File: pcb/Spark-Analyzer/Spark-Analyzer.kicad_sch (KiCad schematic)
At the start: 8 parts, among them J3 KF350-3.5-2P

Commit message: Updated name to Spark Analyzer
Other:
- title: PowerPod -> Spark Analyzer
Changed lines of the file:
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@@
   (paper "A3")
   (title_block
-    (title "PowerPod")
-    (date "2023-04-18")
-    (rev "A")
+    (title "Spark Analyzer")
+    (date "2023-10-06")
+    (rev "B")
   )
   (junction (at 162.56 77.47) (diameter 0) (color 0 0 0 0)
@@
     (pin "1")
     (instances
-      (project "PowerPod"
+      (project "Spark-Analyzer"
         (path "/e63e39d7-6ac0-4ffd-8aa3-1841a4541b55"
           (reference "#PWR04") (unit 1)
@@
     (pin "1")
     (instances
-      (project "PowerPod"
+      (project "Spark-Analyzer"
         (path "/e63e39d7-6ac0-4ffd-8aa3-1841a4541b55"
           (reference "#PWR031") (unit 1)
@@
     (pin "2")
     (instances
-      (project "PowerPod"
+      (project "Spark-Analyzer"
         (path "/e63e39d7-6ac0-4ffd-8aa3-1841a4541b55"
           (reference "J3") (unit 1)
@@
     )
     (instances
-      (project "PowerPod"
+      (project "Spark-Analyzer"
         (path "/e63e39d7-6ac0-4ffd-8aa3-1841a4541b55"
           (reference "H4") (unit 1)
@@
     (pin "1")
     (instances
-      (project "PowerPod"
+      (project "Spark-Analyzer"
         (path "/e63e39d7-6ac0-4ffd-8aa3-1841a4541b55/dc0e84e0-adcd-432b-9bb1-644eba2790b5"
           (reference "TP5") (unit 1)
@@
     )
     (instances
-      (project "PowerPod"
+      (project "Spark-Analyzer"
         (path "/e63e39d7-6ac0-4ffd-8aa3-1841a4541b55"
           (reference "H1") (unit 1)
@@
     (pin "1")
     (instances
-      (project "PowerPod"
+      (project "Spark-Analyzer"
         (path "/e63e39d7-6ac0-4ffd-8aa3-1841a4541b55"
           (reference "#PWR01") (unit 1)
@@
     )
     (instances
-      (project "PowerPod"
+      (project "Spark-Analyzer"
         (path "/e63e39d7-6ac0-4ffd-8aa3-1841a4541b55"
           (reference "H2") (unit 1)
@@
     (pin "2")
     (instances
-      (project "PowerPod"
+      (project "Spark-Analyzer"
         (path "/e63e39d7-6ac0-4ffd-8aa3-1841a4541b55/8b971fa9-4de7-4202-8255-0a278e8cf0e6"
           (reference "C21") (unit 1)
@@
     (pin "2")
     (instances
-      (project "PowerPod"
+      (project "Spark-Analyzer"
         (path "/e63e39d7-6ac0-4ffd-8aa3-1841a4541b55/8b971fa9-4de7-4202-8255-0a278e8cf0e6"
           (reference "C21") (unit 1)
@@
     )
     (instances
-      (project "PowerPod"
+      (project "Spark-Analyzer"
         (path "/e63e39d7-6ac0-4ffd-8aa3-1841a4541b55"
           (reference "H3") (unit 1)
@@
     )
     (instances
-      (project "PowerPod"
+      (project "Spark-Analyzer"
         (path "/e63e39d7-6ac0-4ffd-8aa3-1841a4541b55" (page "4"))
       )
@@
     )
     (instances
-      (project "PowerPod"
+      (project "Spark-Analyzer"
         (path "/e63e39d7-6ac0-4ffd-8aa3-1841a4541b55" (page "2"))
       )
@@
     )
     (instances
-      (project "PowerPod"
+      (project "Spark-Analyzer"
         (path "/e63e39d7-6ac0-4ffd-8aa3-1841a4541b55" (page "5"))
       )
@@
     )
     (instances
-      (project "PowerPod"
+      (project "Spark-Analyzer"
         (path "/e63e39d7-6ac0-4ffd-8aa3-1841a4541b55" (page "3"))
       )

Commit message: First app release and updated PCBA
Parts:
- removed TP5: TestPoint, TestPoint:TestPoint_Pad_D1.0mm, symbol Connector:TestPoint
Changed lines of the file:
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@@
   (junction (at 179.07 77.47) (diameter 0) (color 0 0 0 0)
   )
-  (junction (at 241.3 124.46) (diameter 0) (color 0 0 0 0)
-  )
   (junction (at 280.035 124.46) (diameter 0) (color 0 0 0 0)
   )
@@
     (stroke (width 0) (type default))
   )
-  (wire (pts (xy 241.3 114.935) (xy 241.3 124.46))
-    (stroke (width 0) (type default))
-  )
   (wire (pts (xy 280.035 124.46) (xy 299.72 124.46))
     (stroke (width 0) (type default))
@@
     (stroke (width 0) (type default))
   )
-  (wire (pts (xy 241.3 124.46) (xy 264.795 124.46))
-    (stroke (width 0) (type default))
-  )
   (wire (pts (xy 156.21 99.06) (xy 163.195 99.06))
     (stroke (width 0) (type default))
@@
     (stroke (width 0) (type default))
   )
-  (wire (pts (xy 216.535 124.46) (xy 241.3 124.46))
+  (wire (pts (xy 216.535 124.46) (xy 264.795 124.46))
     (stroke (width 0) (type default))
   )
@@
         )
       )
-    )
-  )
-  (symbol (lib_id "Connector:TestPoint") (at 241.3 114.935 0) (unit 1)
-    (in_bom yes) (on_board yes) (dnp no) (fields_autoplaced)
-    (property "Reference" "TP5" (at 242.697 110.9893 0)
-      (effects (font (size 1.27 1.27)) (justify left))
-    )
-    (property "Value" "TestPoint" (at 242.697 112.9103 0)
-      (effects (font (size 1.27 1.27)) (justify left))
-    )
-    (property "Footprint" "TestPoint:TestPoint_Pad_D1.0mm" (at 246.38 114.935 0)
-      (effects (font (size 1.27 1.27)) hide)
-    )
-    (property "Datasheet" "~" (at 246.38 114.935 0)
-      (effects (font (size 1.27 1.27)) hide)
-    )
-    (pin "1")
-    (instances
-      (project "Spark-Analyzer"
-        (path "/e63e39d7-6ac0-4ffd-8aa3-1841a4541b55/dc0e84e0-adcd-432b-9bb1-644eba2790b5"
-          (reference "TP5") (unit 1)
-        )
-        (path "/e63e39d7-6ac0-4ffd-8aa3-1841a4541b55"
-          (reference "TP9") (unit 1)
-        )
-      )

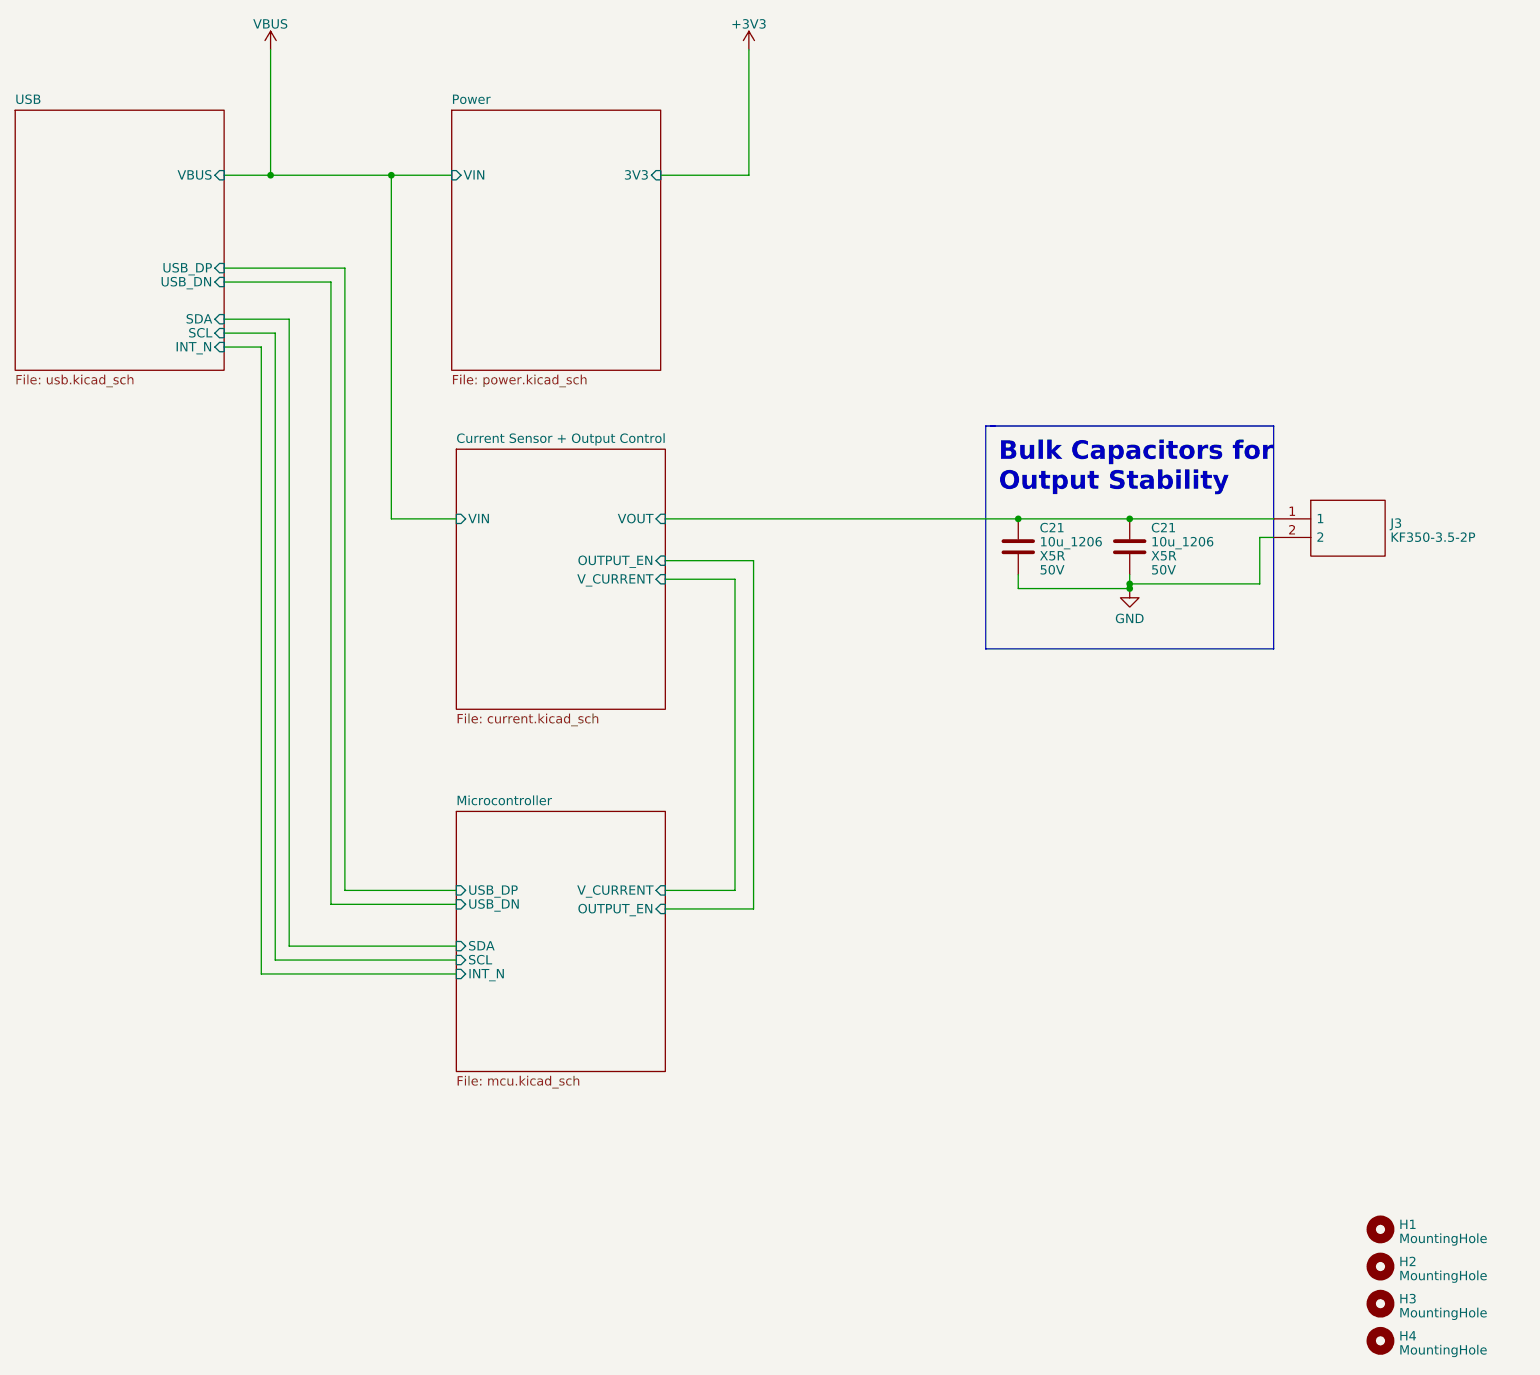
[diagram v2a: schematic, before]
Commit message: Wired sensor and changed connector
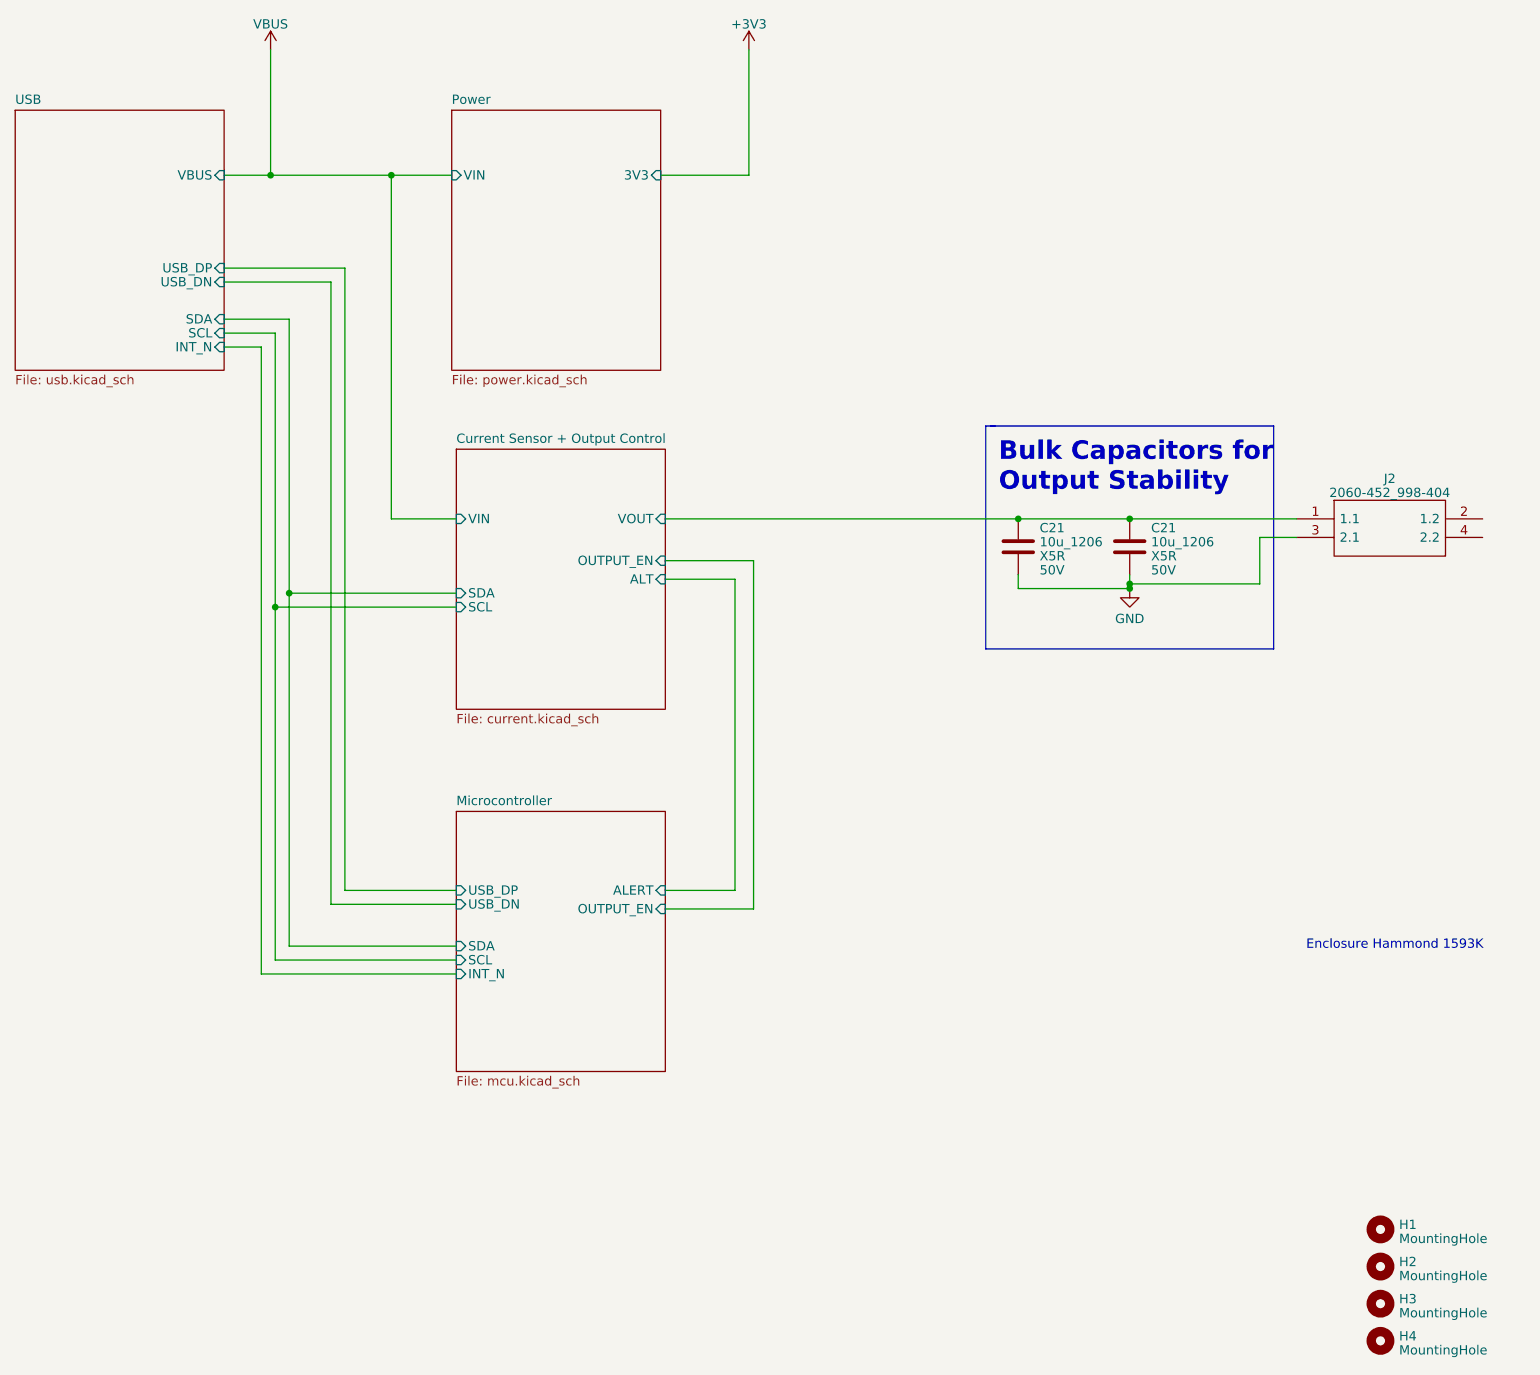
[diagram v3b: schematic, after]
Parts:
- removed J3: KF350-3.5-2P, KF350352P, symbol Connector_JLC:KF350-3.5-2P
- added J2: 2060-452_998-404, 2060452998404, symbol Connector_JLC:2060-452_998-404
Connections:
- net Current Sensor + Output Control/VOUT: now also J2.1 (1.1)
- net GND: now also J2.3 (2.1)
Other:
- sheet Current Sensor + Output Control ports: added ALT, SCL, SDA; removed V_CURRENT
- sheet Microcontroller ports: added ALERT; removed V_CURRENT
- note added: "Enclosure Hammond 1593K"
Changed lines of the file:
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@@
   (junction (at 162.56 77.47) (diameter 0) (color 0 0 0 0)
   )
+  (junction (at 163.195 136.525) (diameter 0) (color 0 0 0 0)
+  )
   (junction (at 264.795 124.46) (diameter 0) (color 0 0 0 0)
   )
@@
   (junction (at 179.07 77.47) (diameter 0) (color 0 0 0 0)
   )
+  (junction (at 165.1 134.62) (diameter 0) (color 0 0 0 0)
+  )
   (junction (at 280.035 124.46) (diameter 0) (color 0 0 0 0)
   )
   (junction (at 280.035 133.35) (diameter 0) (color 0 0 0 0)
   )
-  (wire (pts (xy 299.72 127) (xy 297.815 127))
+  (wire (pts (xy 297.815 127) (xy 302.895 127))
     (stroke (width 0) (type default))
   )
@@
     (stroke (width 0) (type default))
   )
-  (wire (pts (xy 280.035 124.46) (xy 299.72 124.46))
+  (wire (pts (xy 280.035 124.46) (xy 302.895 124.46))
     (stroke (width 0) (type default))
   )
@@
     (stroke (width 0) (type default))
   )
+  (wire (pts (xy 165.1 134.62) (xy 165.1 97.155))
+    (stroke (width 0) (type default))
+  )
   (wire (pts (xy 264.795 124.46) (xy 280.035 124.46))
     (stroke (width 0) (type default))
   )
-  (wire (pts (xy 165.1 182.88) (xy 165.1 97.155))
+  (wire (pts (xy 163.195 136.525) (xy 187.96 136.525))
+    (stroke (width 0) (type default))
+  )
+  (wire (pts (xy 165.1 182.88) (xy 165.1 134.62))
+    (stroke (width 0) (type default))
+  )
+  (wire (pts (xy 165.1 134.62) (xy 187.96 134.62))
     (stroke (width 0) (type default))
   )
@@
     (stroke (width 0) (type default))
   )
-  (wire (pts (xy 163.195 99.06) (xy 163.195 184.785))
+  (wire (pts (xy 163.195 99.06) (xy 163.195 136.525))
     (stroke (width 0) (type default))
   )
@@
   )
   (wire (pts (xy 162.56 60.325) (xy 162.56 77.47))
+    (stroke (width 0) (type default))
+  )
+  (wire (pts (xy 163.195 136.525) (xy 163.195 184.785))
     (stroke (width 0) (type default))
   )
@@
     (effects (font (size 2.54 2.54) (thickness 0.508) bold) (justify left bottom))
   )
+  (text "Enclosure Hammond 1593K" (at 304.165 183.515 0)
+    (effects (font (size 1.27 1.27)) (justify left bottom))
+  )
+  (symbol (lib_id "Connector_JLC:2060-452_998-404") (at 302.895 124.46 0) (unit 1)
+    (in_bom yes) (on_board yes) (dnp no) (fields_autoplaced)
+    (property "Reference" "J2" (at 315.595 118.9609 0)
+      (effects (font (size 1.27 1.27)))
+    )
+    (property "Value" "2060-452_998-404" (at 315.595 120.8819 0)
+      (effects (font (size 1.27 1.27)))
+    )
+    (property "Footprint" "2060452998404" (at 324.485 121.92 0)
+      (effects (font (size 1.27 1.27)) (justify left) hide)
+    )
+    (property "Datasheet" "https://www.wago.com/2060-452/998-404" (at 324.485 124.46 0)
+      (effects (font (size 1.27 1.27)) (justify left) hide)
+    )
+    (property "Description" "SMD PCB terminal block; push-button; 0.75 mm; Pin spacing 4 mm; 2-pole; Push-in CAGE CLAMP; in tape-and-reel packaging" (at 324.485 127 0)
+      (effects (font (size 1.27 1.27)) (justify left) hide)
+    )
+    (property "Height" "4.5" (at 324.485 129.54 0)
+      (effects (font (size 1.27 1.27)) (justify left) hide)
+    )
+    (property "Manufacturer_Name" "Wago" (at 324.485 132.08 0)
+      (effects (font (size 1.27 1.27)) (justify left) hide)
+    )
+    (property "Manufacturer_Part_Number" "2060-452/998-404" (at 324.485 134.62 0)
+      (effects (font (size 1.27 1.27)) (justify left) hide)
+    )
+    (property "Mouser Part Number" "" (at 324.485 137.16 0)
+      (effects (font (size 1.27 1.27)) (justify left) hide)
+    )
+    (property "Mouser Price/Stock" "" (at 324.485 139.7 0)
+      (effects (font (size 1.27 1.27)) (justify left) hide)
+    )
+    (property "Arrow Part Number" "2060-452/998-404" (at 324.485 142.24 0)
+      (effects (font (size 1.27 1.27)) (justify left) hide)
+    )
+    (property "Arrow Price/Stock" "https://www.arrow.com/en/products/2060-452998-404/wago-kontakttechnik-gmbh?utm_currency=USD&region=europe" (at 324.485 144.78 0)
+      (effects (font (size 1.27 1.27)) (justify left) hide)
+    )
+    (property "LCSC" "C2765055" (at 329.565 137.16 0)
+      (effects (font (size 1.27 1.27)) hide)
+    )
+    (pin "1")
+    (pin "2")
+    (pin "3")
+    (pin "4")
+    (instances
+      (project "Spark-Analyzer"
+        (path "/e63e39d7-6ac0-4ffd-8aa3-1841a4541b55"
+          (reference "J2") (unit 1)
+        )
+      )
+    )
+  )
   (symbol (lib_id "power:VBUS") (at 162.56 60.325 0) (unit 1)
     (in_bom yes) (on_board yes) (dnp no) (fields_autoplaced)
@@
         (path "/e63e39d7-6ac0-4ffd-8aa3-1841a4541b55"
           (reference "#PWR031") (unit 1)
-        )
-      )
-    )
-  )
-  (symbol (lib_id "Connector_JLC:KF350-3.5-2P") (at 299.72 124.46 0) (unit 1)
-    (in_bom yes) (on_board yes) (dnp no) (fields_autoplaced)
-    (property "Reference" "J3" (at 315.6712 125.0863 0)
-      (effects (font (size 1.27 1.27)) (justify left))
-    )
-    (property "Value" "KF350-3.5-2P" (at 315.6712 127.0073 0)
-      (effects (font (size 1.27 1.27)) (justify left))
-    )
-    (property "Footprint" "KF350352P" (at 316.23 121.92 0)
-      (effects (font (size 1.27 1.27)) (justify left) hide)
-    )
-    (property "Datasheet" "https://datasheet.lcsc.com/szlcsc/2001160007_Cixi-Kefa-Elec-KF350-3-5-2P_C474892.pdf" (at 316.23 124.46 0)
-      (effects (font (size 1.27 1.27)) (justify left) hide)
-    )
-    (property "Description" "P=3.5mm Screw terminal RoHS 2 Pos" (at 316.23 127 0)
-      (effects (font (size 1.27 1.27)) (justify left) hide)
-    )
-    (property "Height" "8.8" (at 316.23 129.54 0)
-      (effects (font (size 1.27 1.27)) (justify left) hide)
-    )
-    (property "Manufacturer_Name" "CIXI KEFA ELECTRONICS" (at 316.23 132.08 0)
-      (effects (font (size 1.27 1.27)) (justify left) hide)
-    )
-    (property "Manufacturer_Part_Number" "KF350-3.5-2P" (at 316.23 134.62 0)
-      (effects (font (size 1.27 1.27)) (justify left) hide)
-    )
-    (property "Mouser Part Number" "" (at 316.23 137.16 0)
-      (effects (font (size 1.27 1.27)) (justify left) hide)
-    )
-    (property "Mouser Price/Stock" "" (at 316.23 139.7 0)
-      (effects (font (size 1.27 1.27)) (justify left) hide)
-    )
-    (property "Arrow Part Number" "" (at 316.23 142.24 0)
-      (effects (font (size 1.27 1.27)) (justify left) hide)
-    )
-    (property "Arrow Price/Stock" "" (at 316.23 144.78 0)
-      (effects (font (size 1.27 1.27)) (justify left) hide)
-    )
-    (property "LCSC" "C474892" (at 320.675 137.16 0)
-      (effects (font (size 1.27 1.27)) hide)
-    )
-    (pin "1")
-    (pin "2")
-    (instances
-      (project "Spark-Analyzer"
-        (path "/e63e39d7-6ac0-4ffd-8aa3-1841a4541b55"
-          (reference "J3") (unit 1)
         )
       )
@@
       (effects (font (size 1.27 1.27)) (justify left))
     )
+    (pin "SCL" input (at 187.96 136.525 180)
+      (effects (font (size 1.27 1.27)) (justify left))
+    )
     (pin "VOUT" input (at 216.535 124.46 0)
       (effects (font (size 1.27 1.27)) (justify right))
     )
-    (pin "V_CURRENT" input (at 216.535 132.715 0)
-      (effects (font (size 1.27 1.27)) (justify right))
-    )
     (pin "OUTPUT_EN" input (at 216.535 130.175 0)
+      (effects (font (size 1.27 1.27)) (justify right))
+    )
+    (pin "SDA" input (at 187.96 134.62 180)
+      (effects (font (size 1.27 1.27)) (justify left))
+    )
+    (pin "ALT" input (at 216.535 132.715 0)
       (effects (font (size 1.27 1.27)) (justify right))
     )
@@
       (effects (font (size 1.27 1.27)) (justify left top))
     )
-    (pin "V_CURRENT" input (at 216.535 175.26 0)
-      (effects (font (size 1.27 1.27)) (justify right))
-    )
+    (pin "ALERT" input (at 216.535 175.26 0)
+      (effects (font (size 1.27 1.27)) (justify right))
+    )

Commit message: To be reviewed
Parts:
- renumbered C21 to C1, C21 to C22
